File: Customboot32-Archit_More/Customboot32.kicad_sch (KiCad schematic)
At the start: 50 parts, among them J1 USB_B_Micro, J2 Conn_01x14, J3 Conn_01x14, J4 Conn_01x10, J5 Conn_01x12, J6 Conn_01x12, J7 Conn_01x12, J8 Conn_01x12, Q1 SS8050, Q2 SS8050, SW1 EN, SW2 BOOT, SW3 SW_SPDT, U1 ESP32-WROOM-32D, U2 STM32F103C8T6, U3 AMS1117-3.3, U4 CP2102N-Axx-xQFN28, Y1 Crystal_GND24

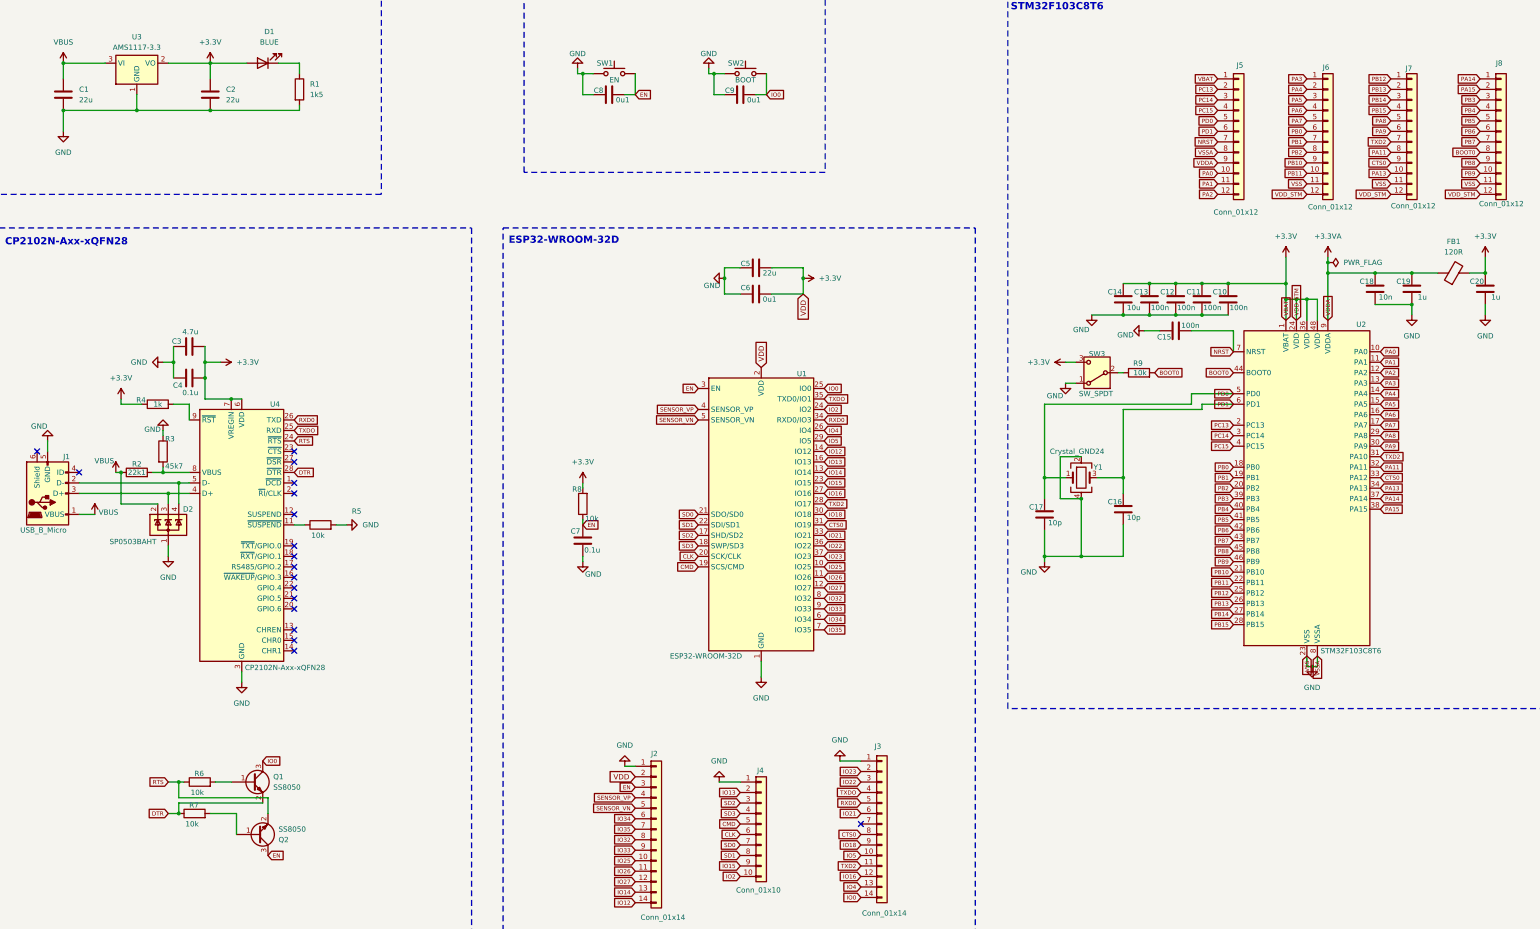
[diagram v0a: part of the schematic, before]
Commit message: ESP OTA code added
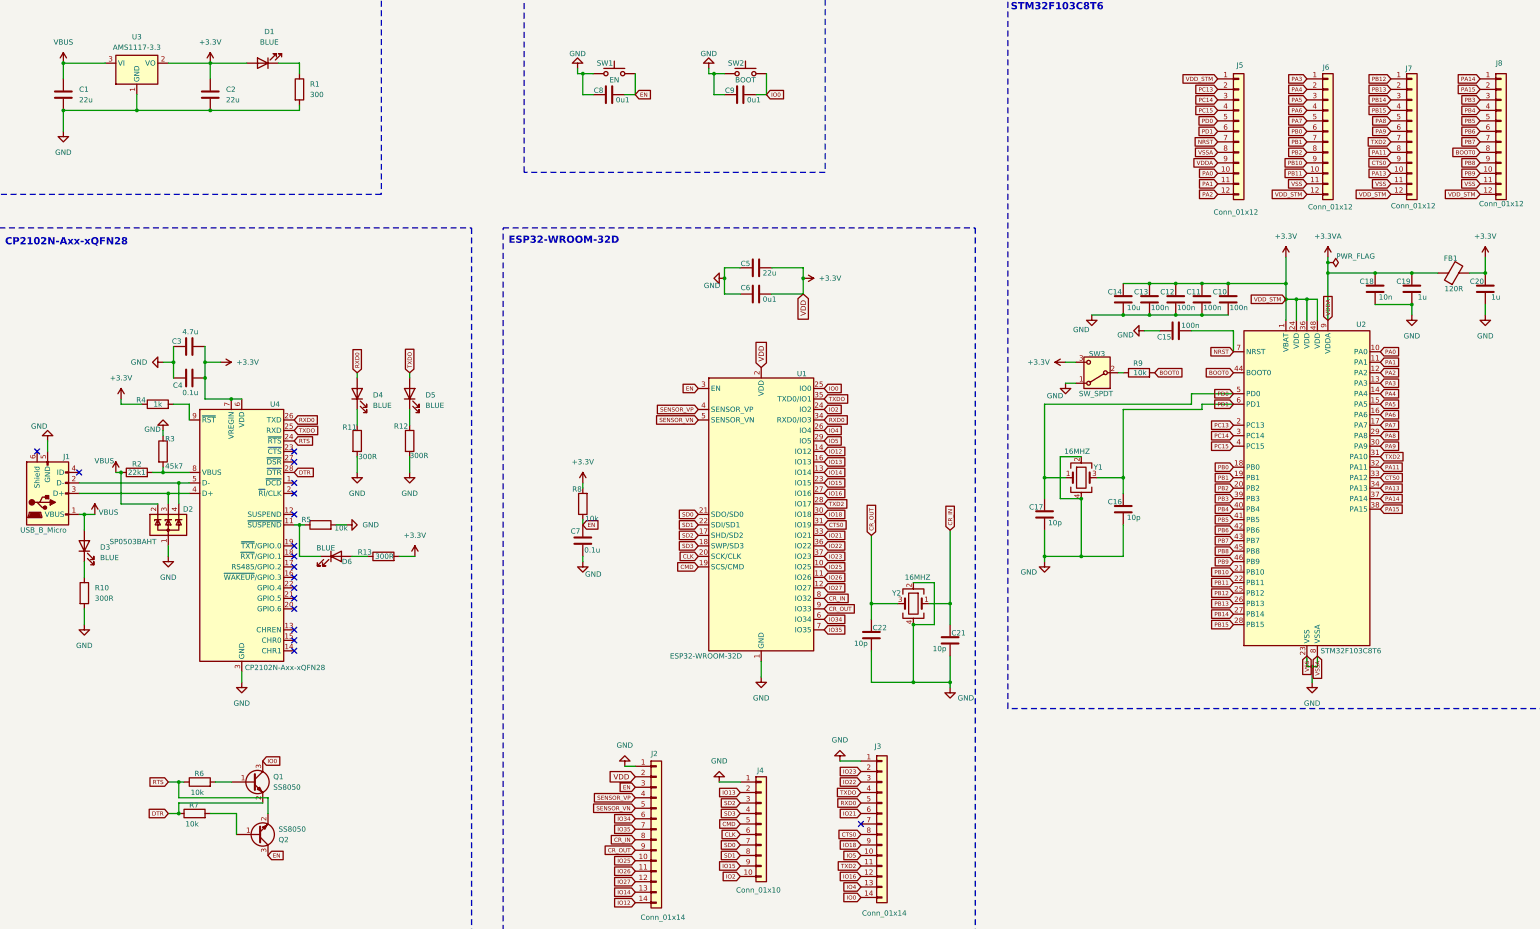
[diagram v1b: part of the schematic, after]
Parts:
- added C21, C22: 10p, symbol Device:C
- added D3, D4, D5, D6: BLUE, symbol Device:LED
- added R10, R11, R12, R13: 300R, symbol Device:R
- added Y2: 16MHZ, symbol Device:Crystal_GND24
- R1: value 1k5 -> 300
- Y1: value Crystal_GND24 -> 16MHZ
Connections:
- net +3.3V: now also R13.2
- net GND: now also C21.1, C22.1, R10.2, R11.2, R12.2, Y2.2, Y2.4
- net RXD0: now also D4.2 (A)
- net TXDO: now also D5.2 (A)
- net VBUS: now also D3.2 (A)
- net at R5.1, U4.11 (~{SUSPEND}): now also D6.1 (K)
- net IO32 renamed CR_IN
- net CR_IN: now also C21.2, Y2.1
- net IO33 renamed CR_OUT
- net CR_OUT: now also C22.2, Y2.3
- new net: D6.2 (A), R13.1
- new net: D4.1 (K), R11.1
- new net: D5.1 (K), R12.1
- new net: D3.1 (K), R10.1
